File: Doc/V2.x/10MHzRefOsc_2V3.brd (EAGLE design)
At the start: 90 x 70 mm, 82 parts, among them CON1 TYCO-AMP_USBUSB-B_SMT, CON2 HEADER-2X5SMD, CON3 SD-73100-0105, CON4 AVR-ISP-6SMD, CON5 AVR-JTAG-10SMD, CON6 HEADER-2X3SMD, CON7 MCX-J-P-X-RA-SM1, U1 ATmega328-P, U2 LC4032V_XXT44, U3 74HCT221D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

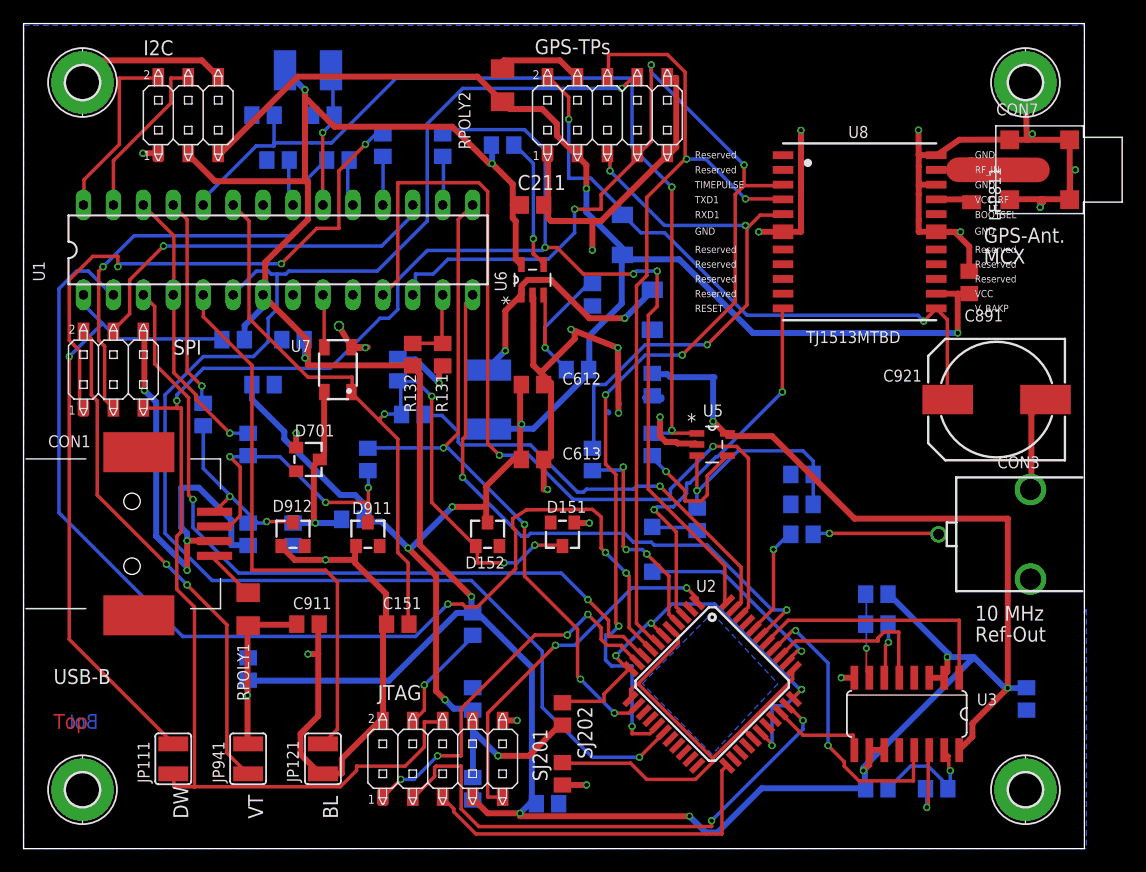
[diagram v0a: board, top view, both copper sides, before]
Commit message: avr_DF4IAH_Bootloader - Doc - Eagle: 2.3 - 3.3V adjusting resistors corrected, 2-way jumpers now THT instead of SMT, GPS-chip package enhanced
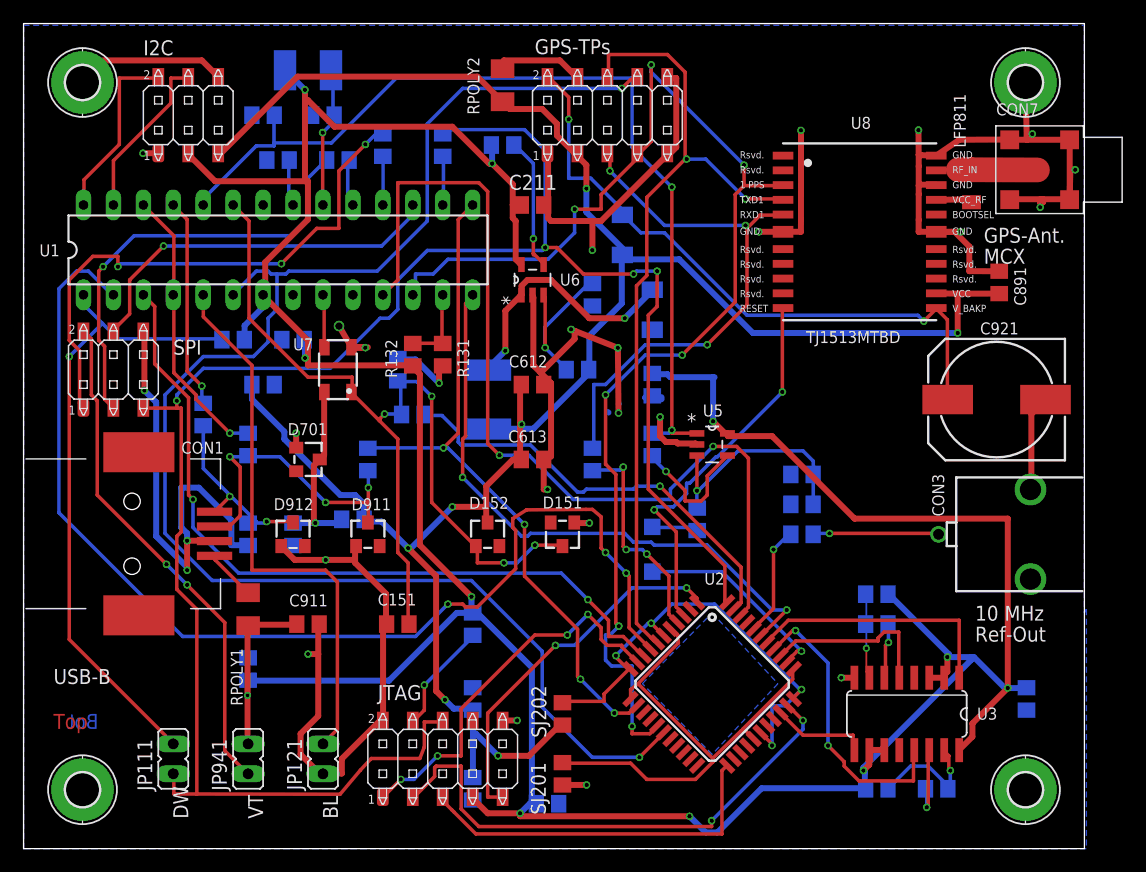
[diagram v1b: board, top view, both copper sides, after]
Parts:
- JP111, JP121, JP941: device jumper:SJW -> jumper:JP1
- R132: value 47k -> 51k
- moved C891 2.54 mm to (82.8, 48.0)
- turned JP111 to 180 degrees
- turned JP121 to 180 degrees
- turned JP941 to 180 degrees
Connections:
- net GND: now also JP121.2; no longer JP121.1
- net INT1: now also JP121.1; no longer JP121.2
- net ISP_VTARGET: now also JP941.2; no longer JP941.1
- net VCC: now also JP941.1; no longer JP941.2
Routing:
- net +3V3: track 181.2 -> 183.7 mm
- net GND: track 262.4 -> 264.8 mm
- net JTAG_SRST: track 162.4 -> 164.2 mm
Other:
- board text added: "DF4IAH 10 MHz Ref.-Osc. V 2.3b"
- board text removed: "DF4IAH 10 MHz Ref.-Osc. V 2.3a"
